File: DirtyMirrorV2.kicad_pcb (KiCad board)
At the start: 2 copper layers, 50 x 50.5 mm, 70 parts, among them J1 PWR, J2 ScopeGroundLoop, SW1 SW_SPDT, U1 TL072, U2 TL074, U3 TL074

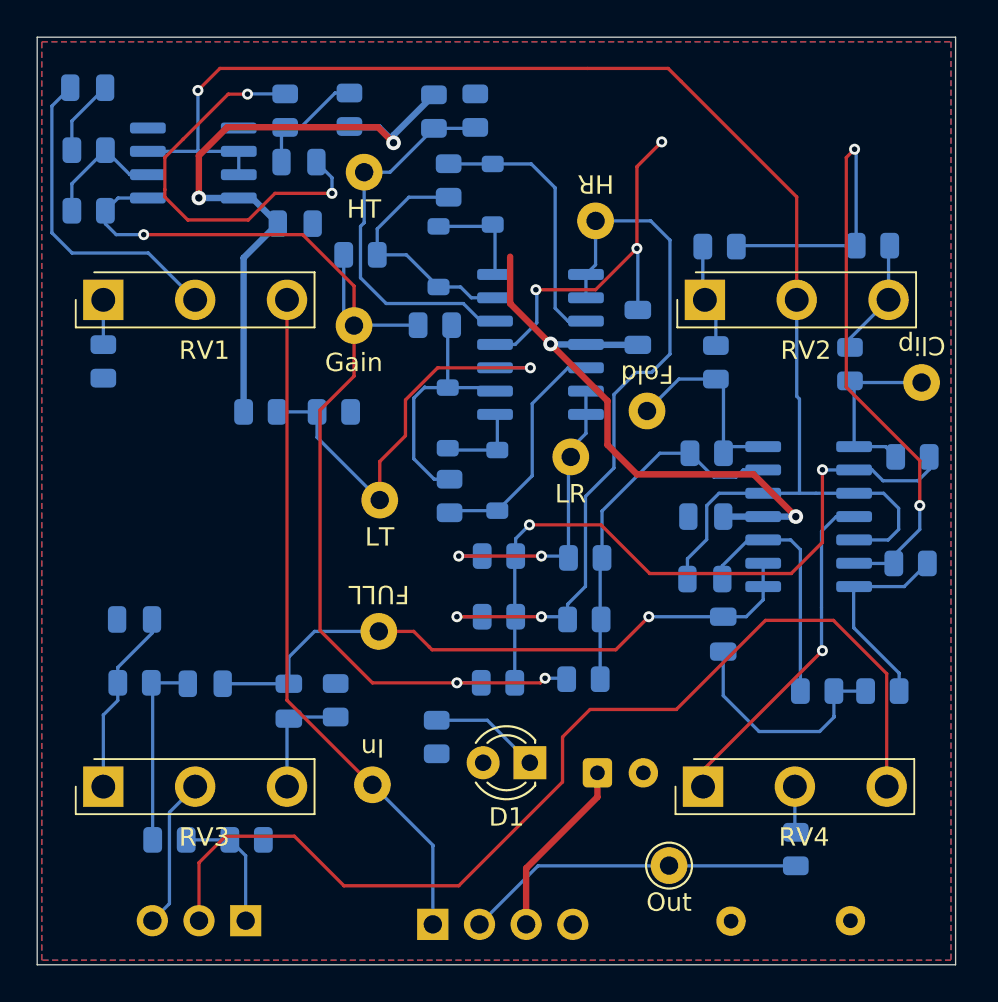
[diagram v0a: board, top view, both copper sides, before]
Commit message: switched to routed power
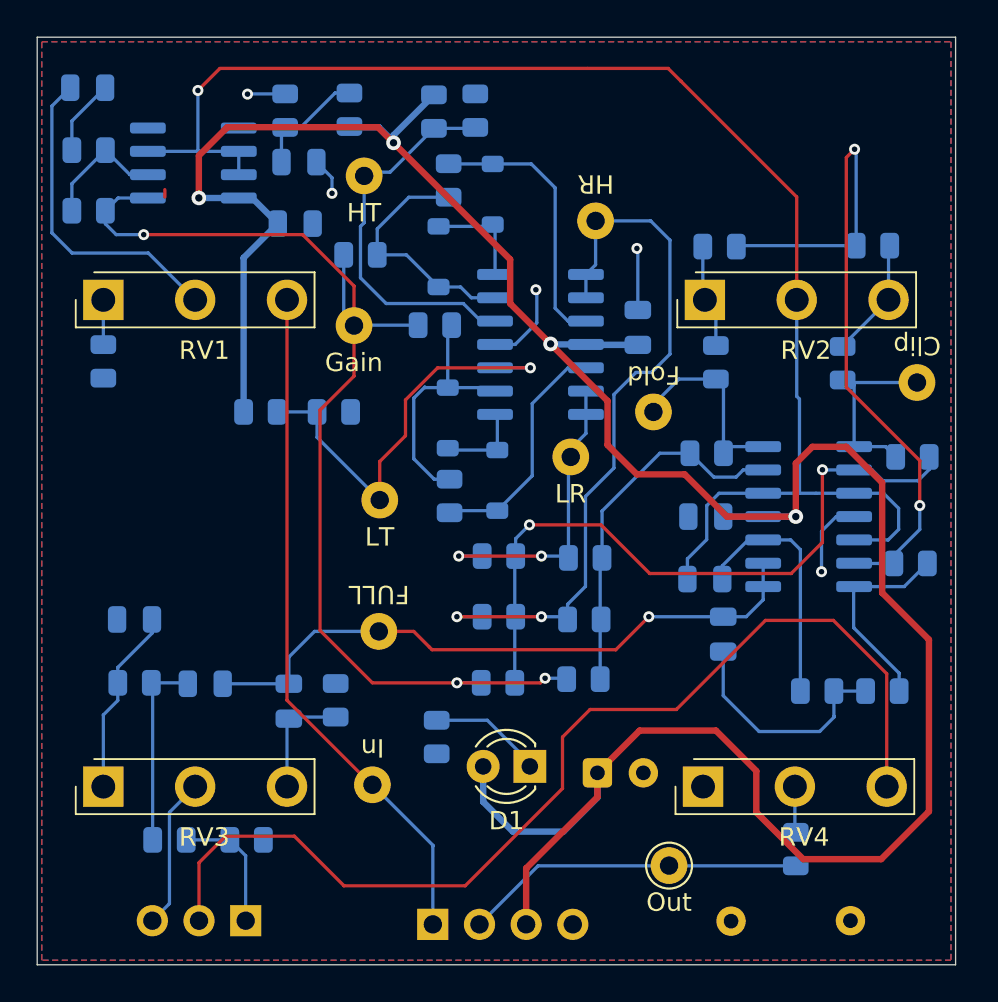
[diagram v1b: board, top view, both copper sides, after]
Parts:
- moved R25 0.40 mm to (40.4, 52.2)
- moved TP3 0.35 mm to (30.1, 54.9)
- moved TP5 0.25 mm to (44.4, 53.3)
- moved D1 0.20 mm to (23.3, 74.2)
- moved TP8 0.20 mm to (14.3, 42.0)
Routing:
- net +9V: track 79.0 -> 150.8 mm
- net 0: track 62.0 -> 17.7 mm, vias 6 -> 5
- added copper zone on F.Cu, net 0
- removed copper zone on F.Cu, net +9V

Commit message: elbow room
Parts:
- moved R27 11.2 mm to (1.20, 67.3), turned to 180 degrees
- moved R28 9.77 mm to (1.30, 71.0), turned to 180 degrees
- moved C10 5.83 mm to (1.20, 60.4)
- moved C8 5.83 mm to (5.05, 63.9)
- moved R29 5.83 mm to (1.20, 63.9)
- moved R10 4.45 mm to (24.8, 38.5)
- moved R9 2.70 mm to (20.8, 38.5)
- moved R22 1.80 mm to (19.8, 62.9)
- moved R20 1.80 mm to (19.8, 66.1)
- moved R21 1.71 mm to (19.9, 69.4)
- moved TP4 0.76 mm to (25.7, 58.1)
- moved R12 0.61 mm to (14.2, 45.8)
- moved R11 0.51 mm to (17.6, 50.3)
- moved TP6 0.40 mm to (14.7, 66.8)
- moved C2 0.11 mm to (27.1, 74.5)
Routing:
- net /Byp: track 7.13 -> 19.8 mm
- net Net-(U3D--): track 39.0 -> 28.8 mm
- net /LoRect: track 16.8 -> 26.3 mm
- net /LowPass: track 10.2 -> 18.5 mm
- net Net-(SW1-B): track 57.3 -> 49.3 mm
- net Net-(C8-Pad2): track 10.6 -> 5.46 mm
- net /FxFull: track 35.0 -> 39.6 mm
- net /HiThresh: track 21.1 -> 24.8 mm, vias 0 -> 1
- net /HiRect: track 39.8 -> 43.4 mm
- net /FxRaw: track 11.2 -> 14.8 mm
- net /Bias: track 81.1 -> 84.0 mm
- net Net-(U3C--): track 37.6 -> 39.6 mm
- net +9V: track 150.8 -> 152.2 mm
- net 0: track 17.7 -> 19.0 mm, vias 5 -> 6
- net /LoThresh: track 23.9 -> 22.8 mm
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
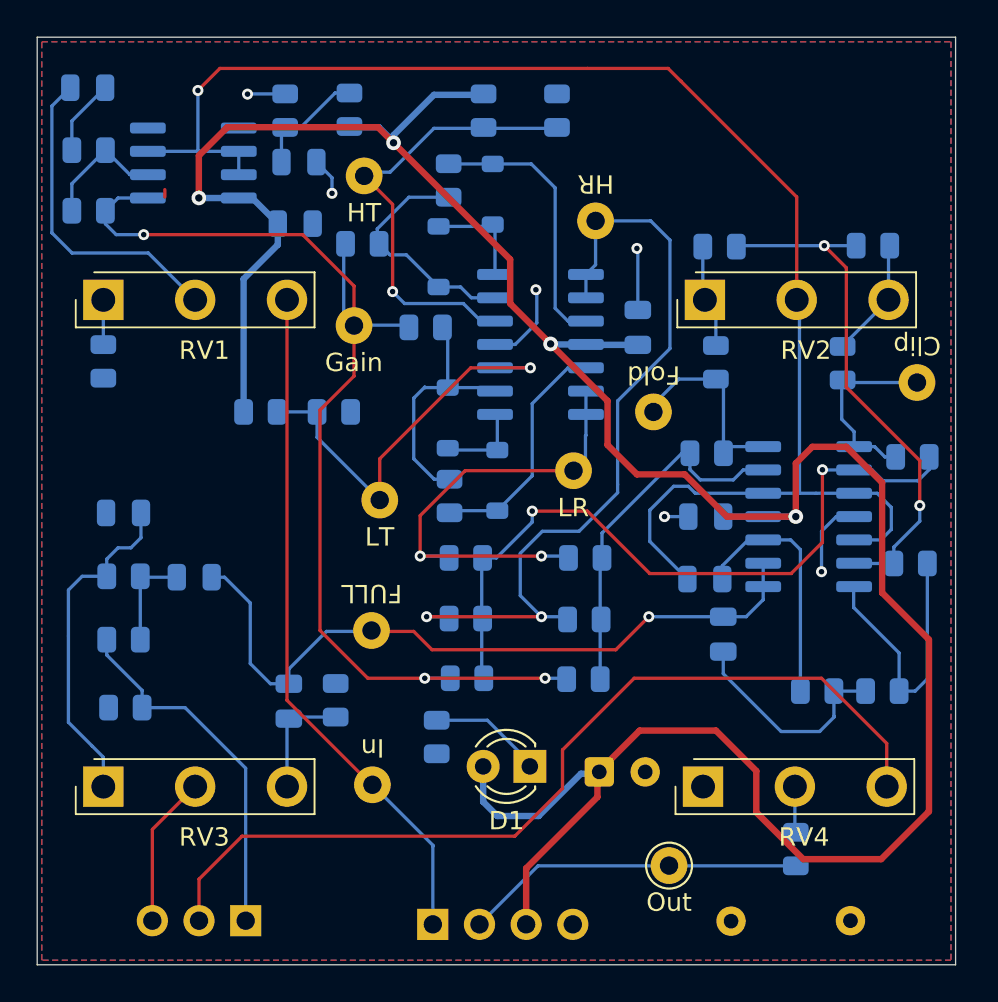
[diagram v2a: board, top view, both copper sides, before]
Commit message: top jacks, new routing
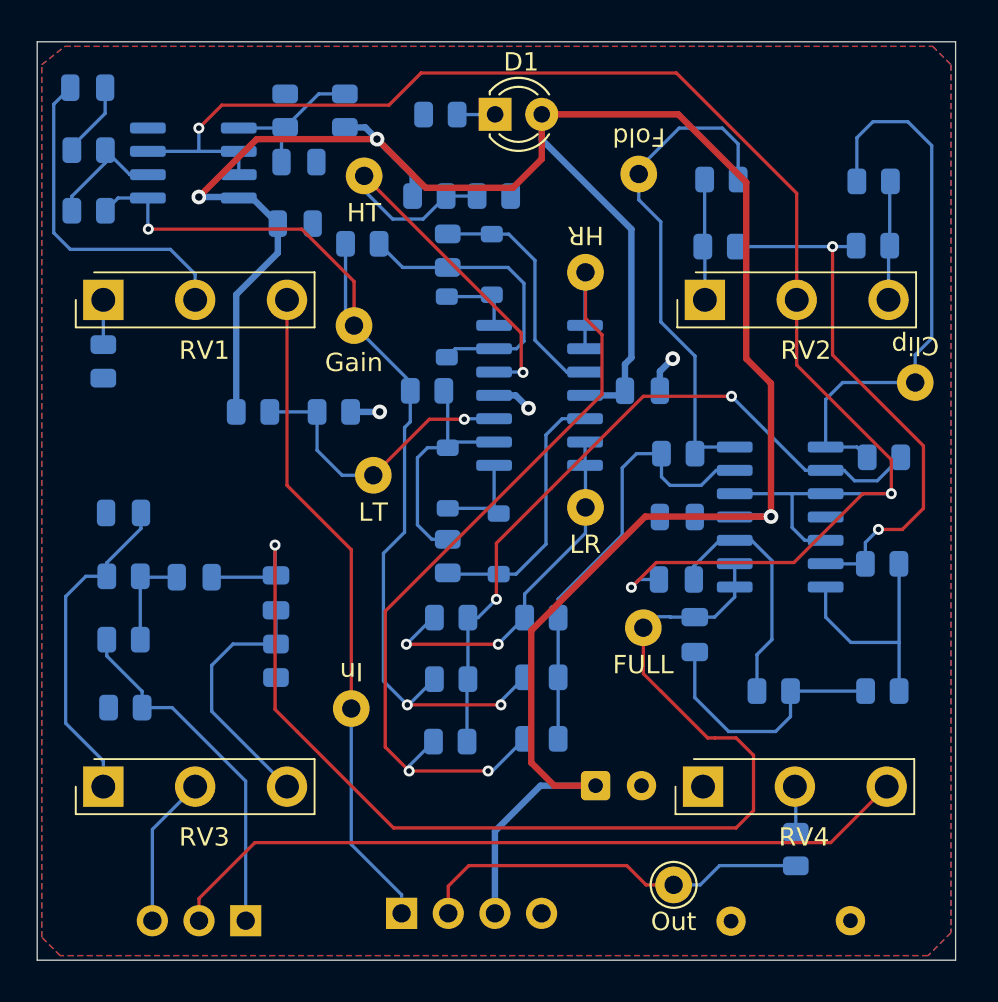
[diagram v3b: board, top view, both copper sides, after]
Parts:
- moved D1 35.6 mm to (21.4, 38.7), turned to 0 degrees
- moved R4 33.9 mm to (18.5, 38.7), turned to 180 degrees
- moved TP6 14.8 mm to (29.5, 66.7), turned to 180 degrees
- moved TP3 13.0 mm to (29.2, 42.0)
- moved R25 10.0 mm to (42.0, 42.4), turned to 0 degrees
- moved R26 9.95 mm to (33.8, 42.2), turned to 180 degrees
- moved R16 6.91 mm to (23.9, 72.7)
- moved R20 6.75 mm to (19.0, 72.8)
- moved C9 5.94 mm to (9.50, 64.8)
- moved R10 5.78 mm to (21.4, 43.1), turned to 0 degrees
- moved R9 5.51 mm to (17.9, 43.1), turned to 0 degrees
- moved TP1 4.31 mm to (13.6, 71.0)
- moved R18 4.03 mm to (23.9, 66.1)
- moved R32 3.90 mm to (9.50, 68.5), turned to -90 degrees
- moved D3 3.85 mm to (18.8, 50.3)
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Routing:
- net /FxFull: track 39.6 -> 64.1 mm
- net /Clip: track 10.7 -> 31.0 mm
- net /Fold: track 10.9 -> 27.7 mm
- net 0: track 19.0 -> 5.79 mm, vias 6 -> 3
- net +9V: track 152.2 -> 139.0 mm, vias 4 -> 3
- net /Bias: track 84.0 -> 92.9 mm, vias 1 -> 3
- net Net-(SW1-B): track 49.3 -> 41.2 mm
- net /HiPass: track 6.33 -> 14.1 mm
- net /LoThresh: track 22.8 -> 16.1 mm
- net /LoRect: track 26.3 -> 20.1 mm
- net /Gain: track 61.5 -> 56.0 mm
- net Net-(U3B--): track 19.9 -> 24.4 mm
- net Net-(D1-K): track 6.23 -> 2.07 mm
- net Net-(D3-K): track 13.0 -> 16.5 mm
- net FX_OUT: track 18.5 -> 21.7 mm
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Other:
- board size 50 x 50.5 mm -> 50 x 50 mm

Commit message: rev1 gerbers ready
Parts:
- moved R34 5.51 mm to (32.4, 79.8)
- moved TP10 2.89 mm to (28.3, 81.1)
- moved TP3 2.25 mm to (27.0, 42.0)
- moved J2 2.04 mm to (39.3, 82.0)
- moved TP6 1.45 mm to (29.2, 68.1)
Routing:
- net +9V: track 139.0 -> 133.4 mm
- net FX_OUT: track 21.7 -> 16.3 mm
- net Net-(R34-Pad1): track 2.51 -> 6.84 mm
- net /Fold: track 27.7 -> 29.8 mm
- net Net-(U3B--): track 24.4 -> 25.4 mm
- net /HiRect: track 46.3 -> 45.5 mm
- net 0: vias 3 -> 16
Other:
- board text added: "+9v"
- board text added: "Dirty Mirror V2"
- board text added: "GND"
- board text added: "Gain"
- board text added: "In"
- board text added: "Out"
- board text added: "Rev 1- 02/2026 Hayden Setlik"
- board text added: "Shape"
- board text added: "Tone"
- board text added: "Volume"

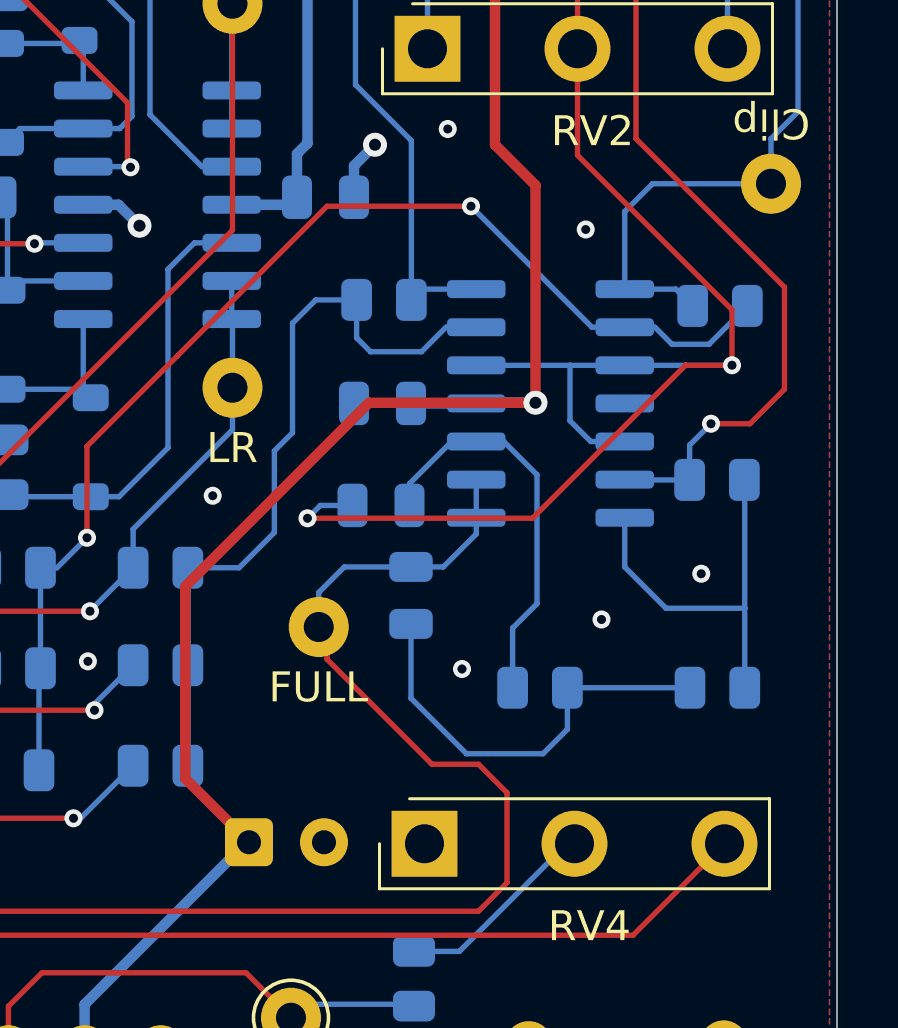
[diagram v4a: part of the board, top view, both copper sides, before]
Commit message: sike minor fix. DRC passing
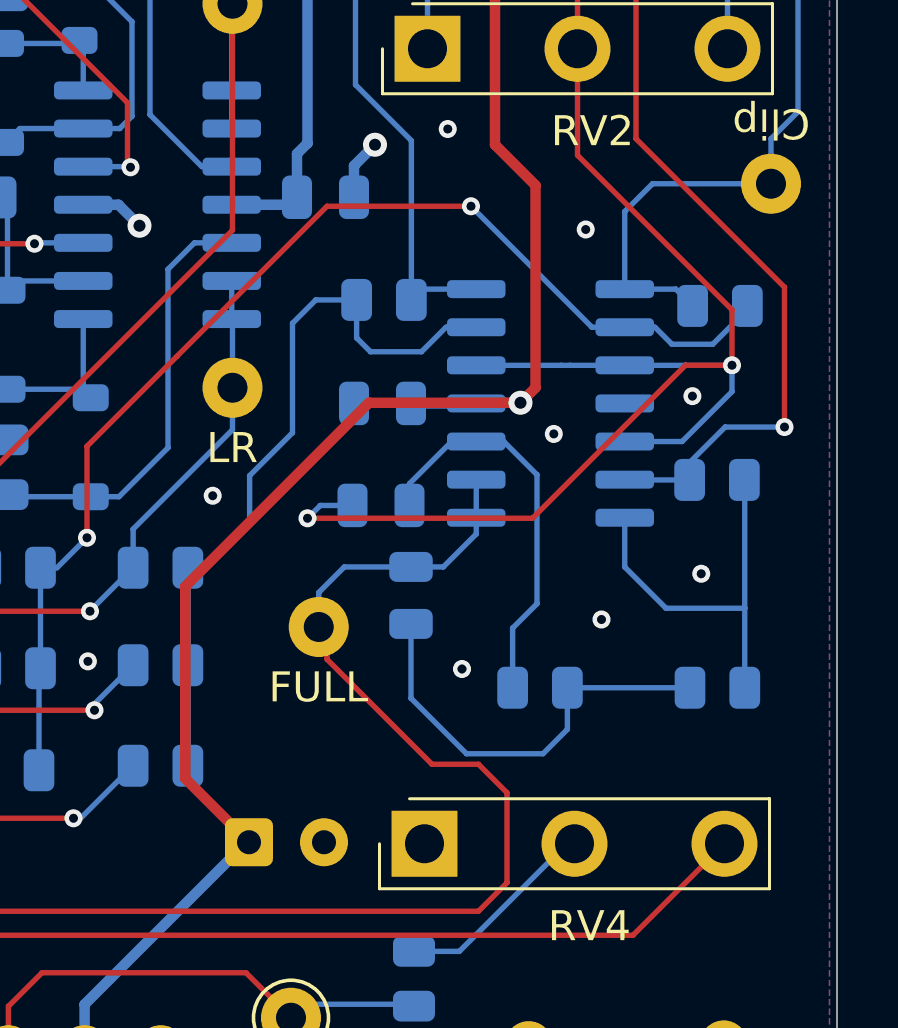
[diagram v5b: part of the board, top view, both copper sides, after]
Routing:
- net /Bias: track 92.9 -> 94.1 mm
- net +9V: track 133.4 -> 132.6 mm
- net Net-(U3B--): track 25.4 -> 24.8 mm
- net 0: vias 16 -> 18

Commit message: value tweaks, added BOM
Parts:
- R24: value 47k -> 33k
- R33: value 100k -> 470k
- R4: value 4k7 -> 6k8

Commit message: resistor values tweaked to taste
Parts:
- R10, R7: value 51k -> 56k
- R23: value 56k -> 100k
- R24: value 33k -> 82k
- R27: value 100k -> 47k
- R3: value 4k7 -> 22k
- R5: value 27k -> 22k
- R8, R9: value 39k -> 47k
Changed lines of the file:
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@@
 			)
 		)
-		(property "Sim.Params" "wpos=0.2 Rtot=100k"
+		(property "Sim.Params" "wpos=0.2 Rtot=10k"
 			(at 0 0 0)
 			(unlocked yes)
@@
 			)
 		)
-		(property "Value" "33k"
+		(property "Value" "82k"
 			(at 0 -1.65 0)
 			(layer "B.Fab")
@@
 			)
 		)
-		(property "Value" "39k"
+		(property "Value" "47k"
 			(at 0 -1.65 180)
 			(layer "B.Fab")
@@
 			)
 		)
-		(property "Value" "100k"
+		(property "Value" "47k"
 			(at 0 -1.65 0)
 			(layer "B.Fab")
@@
 			)
 		)
-		(property "Value" "27k"
+		(property "Value" "22k"
 			(at 0 -1.65 0)
 			(layer "B.Fab")
@@
 			)
 		)
-		(property "Value" "51k"
+		(property "Value" "56k"
 			(at 0 -1.65 180)
 			(layer "B.Fab")
@@
 			)
 		)
-		(property "Value" "51k"
+		(property "Value" "56k"
 			(at 0 -1.65 0)
 			(layer "B.Fab")
@@
 			)
 		)
-		(property "Value" "39k"
+		(property "Value" "47k"
 			(at 0 -1.65 0)
 			(layer "B.Fab")
@@
 			)
 		)
-		(property "Value" "4k7"
+		(property "Value" "22k"
 			(at 0 -1.65 90)
 			(layer "B.Fab")
@@
 			)
 		)
-		(property "Value" "56k"
+		(property "Value" "100k"
 			(at 0 -1.65 0)
 			(layer "B.Fab")
